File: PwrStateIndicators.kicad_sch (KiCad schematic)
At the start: 12 parts, among them J14 Motor-P, J15 Motor-C, J16 Array-C, J17 Array-P, U10 EL3H7, U11 EL3H7, U8 EL3H7, U9 EL3H7

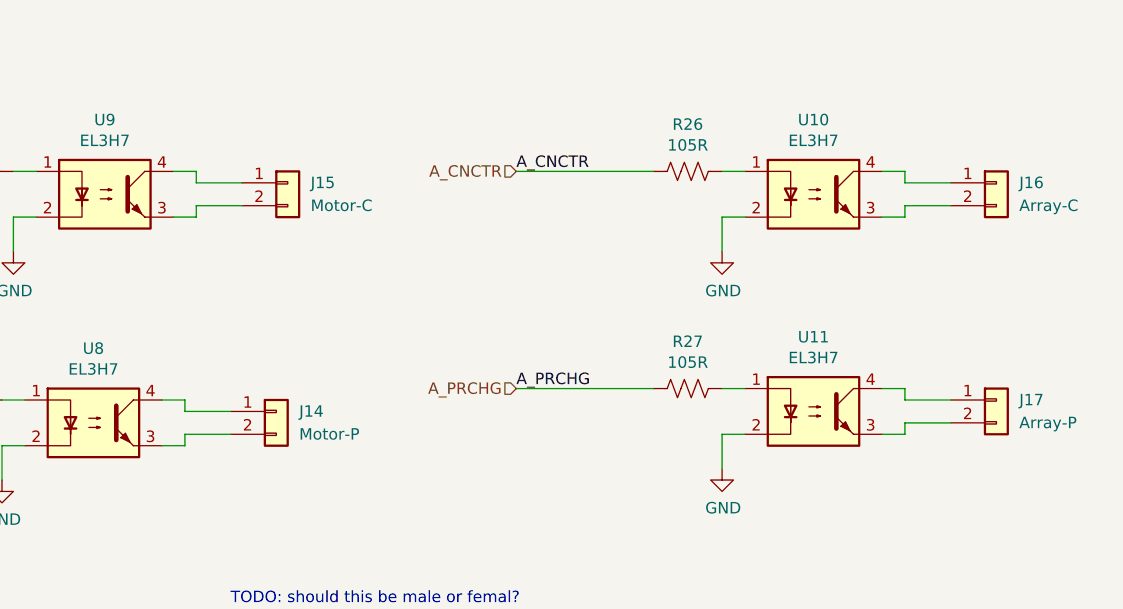
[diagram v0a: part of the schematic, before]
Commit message: Remove 12V isolator, swap CAN connector pins, etc.
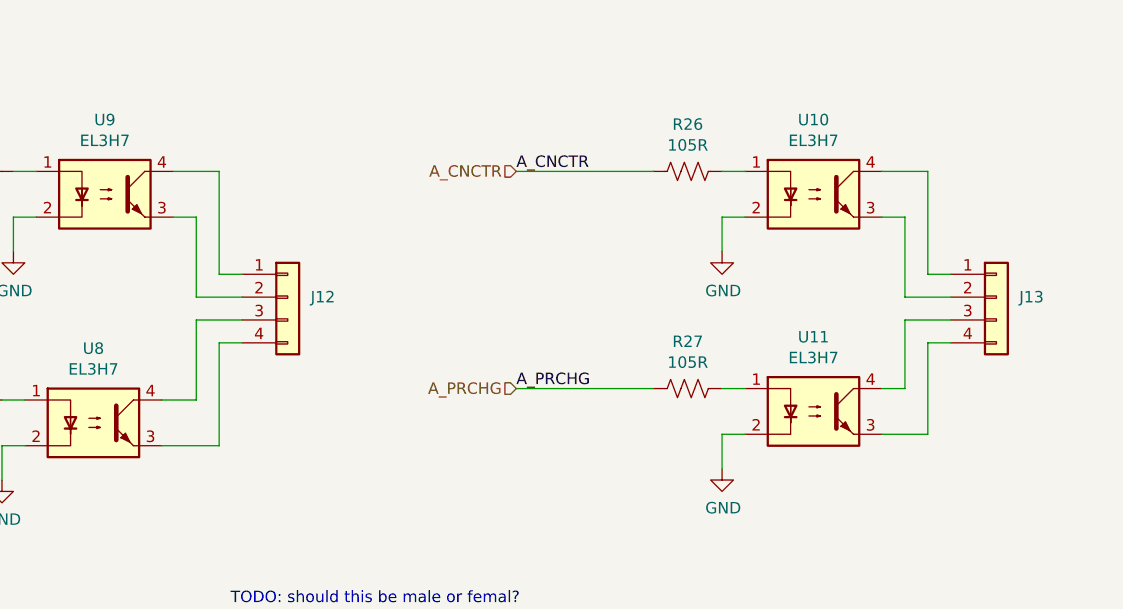
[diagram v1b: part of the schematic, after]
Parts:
- removed J14: Motor-P, UTSVT_Connectors:Molex_MicroFit3.0_1x2xP3.00mm_PolarizingPeg_Vertical, symbol Connector_Generic:Conn_01x02
- removed J15: Motor-C, UTSVT_Connectors:Molex_MicroFit3.0_1x2xP3.00mm_PolarizingPeg_Vertical, symbol Connector_Generic:Conn_01x02
- removed J16: Array-C, UTSVT_Connectors:Molex_MicroFit3.0_1x2xP3.00mm_PolarizingPeg_Vertical, symbol Connector_Generic:Conn_01x02
- removed J17: Array-P, UTSVT_Connectors:Molex_MicroFit3.0_1x2xP3.00mm_PolarizingPeg_Vertical, symbol Connector_Generic:Conn_01x02
- added J12, J13: (no value), symbol Connector_Generic:Conn_01x04
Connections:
- net at U11.3: now also J13.4 (Pin_4)
- net at U11.4: now also J13.3 (Pin_3)
- net at U8.3: now also J12.4 (Pin_4)
- net at U8.4: now also J12.3 (Pin_3)
- net at U9.3: now also J12.2 (Pin_2)
- net at U9.4: now also J12.1 (Pin_1)
- net at U10.3: now also J13.2 (Pin_2)
- net at U10.4: now also J13.1 (Pin_1)

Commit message: Release v2.4 and gerbers
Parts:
- J12, J13: value (none) -> Conn_01x04; footprint (none) -> Connector_Molex:Molex_Micro-Fit_3.0_43650-0415_1x04_P3.00mm_Vertical
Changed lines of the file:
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@@
       (effects (font (size 1.27 1.27)) (justify left))
     )
-    (property "Value" "" (id 1) (at 212.09 109.2199 0)
+    (property "Value" "Conn_01x04" (id 1) (at 212.09 109.2199 0)
       (effects (font (size 1.27 1.27)) (justify left))
     )
-    (property "Footprint" "" (id 2) (at 209.55 106.68 0)
+    (property "Footprint" "Connector_Molex:Molex_Micro-Fit_3.0_43650-0415_1x04_P3.00mm_Vertical" (id 2) (at 209.55 106.68 0)
       (effects (font (size 1.27 1.27)) hide)
     )
@@
       (effects (font (size 1.27 1.27)) (justify left))
     )
-    (property "Value" "" (id 1) (at 133.35 109.2199 0)
+    (property "Value" "Conn_01x04" (id 1) (at 133.35 109.2199 0)
       (effects (font (size 1.27 1.27)) (justify left))
     )
-    (property "Footprint" "" (id 2) (at 130.81 106.68 0)
+    (property "Footprint" "Connector_Molex:Molex_Micro-Fit_3.0_43650-0415_1x04_P3.00mm_Vertical" (id 2) (at 130.81 106.68 0)
       (effects (font (size 1.27 1.27)) hide)
     )

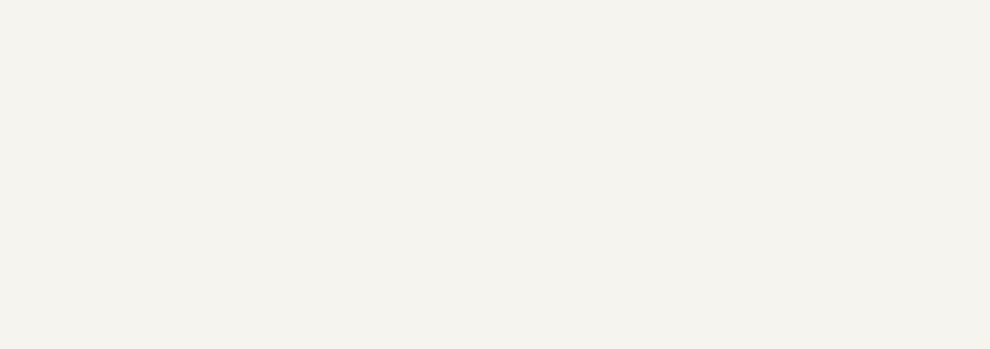
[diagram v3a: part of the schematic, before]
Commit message: Updated schematic in accordance to previous weeks annotated changes
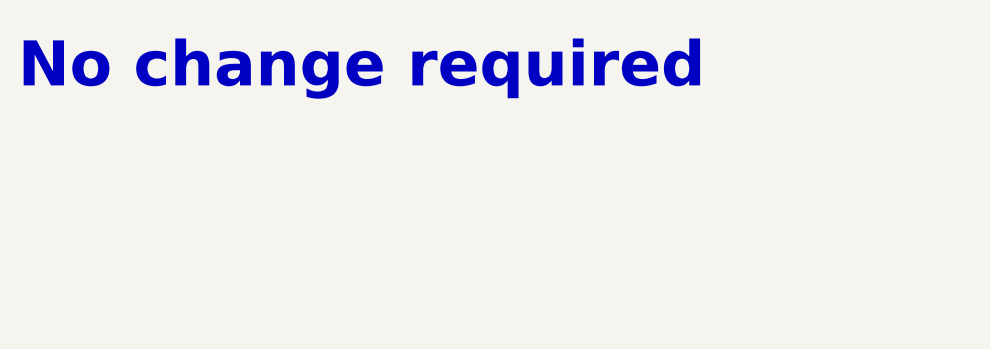
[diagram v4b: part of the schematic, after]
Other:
- note added: "No change required"
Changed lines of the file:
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@@
     (effects (font (size 2.54 2.54) (thickness 0.508) bold) (justify left bottom))
+  )
+  (text "No change required\n" (at 15.24 22.86 0)
+    (effects (font (face "KiCad Font") (size 5 5) (thickness 1) bold (color 255 2 13 1)) (justify left bottom))
   )
   (label "A_CNCTR" (at 156.21 92.71 0) (fields_autoplaced)

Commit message: Flipped optoisolators, changed resistor values, added second connector to motor can and disconnected shield pins for now since I haven't seen them used (will chack against old version to see what the circuit looked like), copied power-in circuit from contactor board, added optoisolator to timer and blinker light connection.
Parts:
- U10, U11, U8, U9: footprint Package_SO:SOP-4_4.4x2.6mm_P1.27mm -> Package_DIP:DIP-4_W7.62mm
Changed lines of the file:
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@@
 			)
 		)
-		(property "Footprint" "Package_SO:SOP-4_4.4x2.6mm_P1.27mm"
+		(property "Footprint" "Package_DIP:DIP-4_W7.62mm"
 			(at 184.15 124.46 0)
 			(effects
@@
 			)
 		)
-		(property "Datasheet" ""
+		(property "Datasheet" "http://www.vishay.com/docs/83740/sfh617a.pdf"
 			(at 189.23 119.38 0)
 			(effects
@@
 			)
 		)
-		(property "Description" ""
+		(property "Description" "Optocoupler, Phototransistor Output, 5300 VRMS, VCEO 70V, CTR% 40-80, -55 to +110 degree Celsius, UL, BSI, FIMKO, cUL, THT PDIP-4"
 			(at 189.23 119.38 0)
 			(effects
@@
 			)
 		)
-		(property "Description" ""
+		(property "Description" "Resistor, US symbol"
 			(at 175.26 116.84 0)
 			(effects
@@
 			)
 		)
-		(property "Description" ""
+		(property "Description" "Power symbol creates a global label with name \"GND\" , ground"
 			(at 179.07 125.73 0)
 			(effects
@@
 			)
 		)
-		(property "Footprint" "Package_SO:SOP-4_4.4x2.6mm_P1.27mm"
+		(property "Footprint" "Package_DIP:DIP-4_W7.62mm"
 			(at 104.14 125.73 0)
 			(effects
@@
 			)
 		)
-		(property "Datasheet" ""
+		(property "Datasheet" "http://www.vishay.com/docs/83740/sfh617a.pdf"
 			(at 109.22 120.65 0)
 			(effects
@@
 			)
 		)
-		(property "Description" ""
+		(property "Description" "Optocoupler, Phototransistor Output, 5300 VRMS, VCEO 70V, CTR% 40-80, -55 to +110 degree Celsius, UL, BSI, FIMKO, cUL, THT PDIP-4"
 			(at 109.22 120.65 0)
 			(effects
@@
 			)
 		)
-		(property "Description" ""
+		(property "Description" "Resistor, US symbol"
 			(at 95.25 118.11 0)
 			(effects
@@
 			)
 		)
-		(property "Description" ""
+		(property "Description" "Power symbol creates a global label with name \"GND\" , ground"
 			(at 99.06 127 0)
 			(effects
@@
 			)
 		)
-		(property "Footprint" "Package_SO:SOP-4_4.4x2.6mm_P1.27mm"
+		(property "Footprint" "Package_DIP:DIP-4_W7.62mm"
 			(at 105.41 100.33 0)
 			(effects
@@
 			)
 		)
-		(property "Datasheet" ""
+		(property "Datasheet" "http://www.vishay.com/docs/83740/sfh617a.pdf"
 			(at 110.49 95.25 0)
 			(effects
@@
 			)
 		)
-		(property "Description" ""
+		(property "Description" "Optocoupler, Phototransistor Output, 5300 VRMS, VCEO 70V, CTR% 40-80, -55 to +110 degree Celsius, UL, BSI, FIMKO, cUL, THT PDIP-4"
 			(at 110.49 95.25 0)
 			(effects
@@
 			)
 		)
-		(property "Description" ""
+		(property "Description" "Resistor, US symbol"
 			(at 96.52 92.71 0)
 			(effects
@@
 			)
 		)
-		(property "Description" ""
+		(property "Description" "Power symbol creates a global label with name \"GND\" , ground"
 			(at 100.33 101.6 0)
 			(effects
@@
 			)
 		)
-		(property "Footprint" "Package_SO:SOP-4_4.4x2.6mm_P1.27mm"
+		(property "Footprint" "Package_DIP:DIP-4_W7.62mm"
 			(at 184.15 100.33 0)
 			(effects
@@
 			)
 		)
-		(property "Datasheet" ""
+		(property "Datasheet" "http://www.vishay.com/docs/83740/sfh617a.pdf"
 			(at 189.23 95.25 0)
 			(effects
@@
 			)
 		)
-		(property "Description" ""
+		(property "Description" "Optocoupler, Phototransistor Output, 5300 VRMS, VCEO 70V, CTR% 40-80, -55 to +110 degree Celsius, UL, BSI, FIMKO, cUL, THT PDIP-4"
 			(at 189.23 95.25 0)
 			(effects
@@
 			)
 		)
-		(property "Description" ""
+		(property "Description" "Resistor, US symbol"
 			(at 175.26 92.71 0)
 			(effects
@@
 			)
 		)
-		(property "Description" ""
+		(property "Description" "Power symbol creates a global label with name \"GND\" , ground"
 			(at 179.07 101.6 0)
 			(effects
@@
 			)
 		)
-		(property "Description" ""
+		(property "Description" "Generic connector, single row, 01x04, script generated (kicad-library-utils/schlib/autogen/connector/)"
 			(at 209.55 106.68 0)
 			(effects
@@
 			)
 		)
-		(property "Description" ""
+		(property "Description" "Generic connector, single row, 01x04, script generated (kicad-library-utils/schlib/autogen/connector/)"
 			(at 130.81 106.68 0)
 			(effects
